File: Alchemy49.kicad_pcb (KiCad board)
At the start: 2 copper layers, 267.5 x 76.2 mm, 255 parts, among them J1 USB_B_Micro, J2 Conn_01x05_Female, Q1 2N7002E, SW1 ESC-1.5U, SW10 O-1U, SW11 P-1U, SW12 BACK-1.5U, SW13 DEL-1U, SW14 TAB-1.75U, SW15 A-1U, SW16 S-1U, SW17 D-1U, SW18 F-1U, SW19 G-1U, SW2 Q-1U, SW20 H-1U, SW21 J-1U, SW22 K-1U, SW23 L-1U, SW24 ENTER-2.25U, SW25 PGUP-1U, SW26 SHIFT-2U, SW27 Z-1U, SW28 X-1U, SW29 C-1U, SW3 W-1U, SW30 V-1U, SW31 B-1U, SW32 N-1U, SW33 M-1U, SW34 COM-1U, SW35 PER-1U, SW36 SLASH-1U, SW37 UP-1U, SW38 PGDN-1U, SW39 CTRL1-1U, SW4 E-1U, SW40 WIN-1U, SW41 ALT-1U, SW42 FN1-1U, SW43 SPACE-2.75U, SW44 SHIFT-2.25U, SW45 FN2-1U, SW46 CTRL2-1U, SW47 LEFT-1U, SW48 DOWN-1U, SW49 RIGHT-1U, SW5 R-1U, SW6 T-1U, SW7 Y-1U, SW8 U-1U, SW9 I-1U

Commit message: Prototype Adjustments
* Added working KBFirmware config and hex files.
* Added example AVRDUDESS screenshot
* Added datasheet and part numbers to sch
* Adjusted pcb outlin and holes
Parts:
- removed H1, H2: MountingHole_Pad, MountingHole:MountingHole_3.5mm_Pad_Via
- moved D39 0.90 mm to (32.0, 74.5)
- moved J1 0.20 mm to (40.2, 26.5)
- moved J2 0.20 mm to (40.2, 32.5)
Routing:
- net Row1: track 298.9 -> 301.5 mm
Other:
- outline, holes or cut-outs redrawn
- board text added: "B"
- board text added: "G"
- board text added: "R"
- board text added: "Sh"
- board text added: "W"

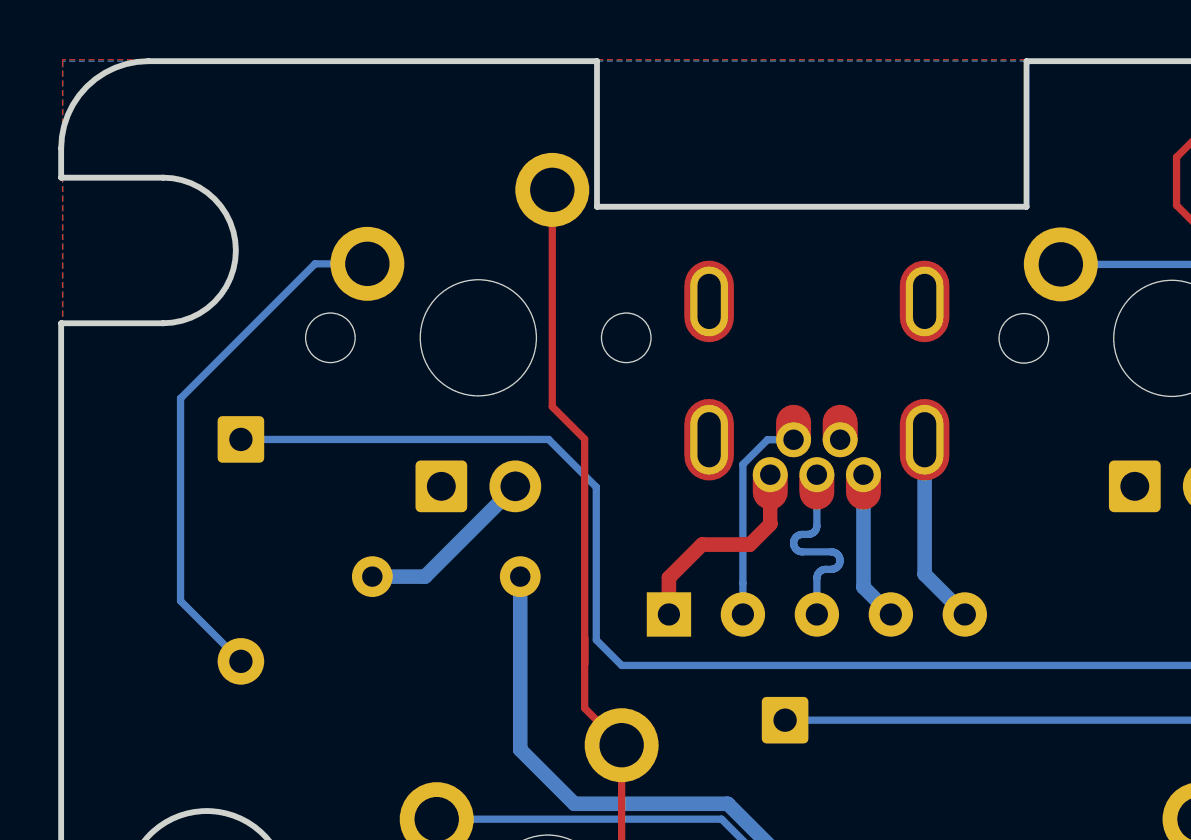
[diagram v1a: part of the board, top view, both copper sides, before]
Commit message: Cut layer adjustments for final
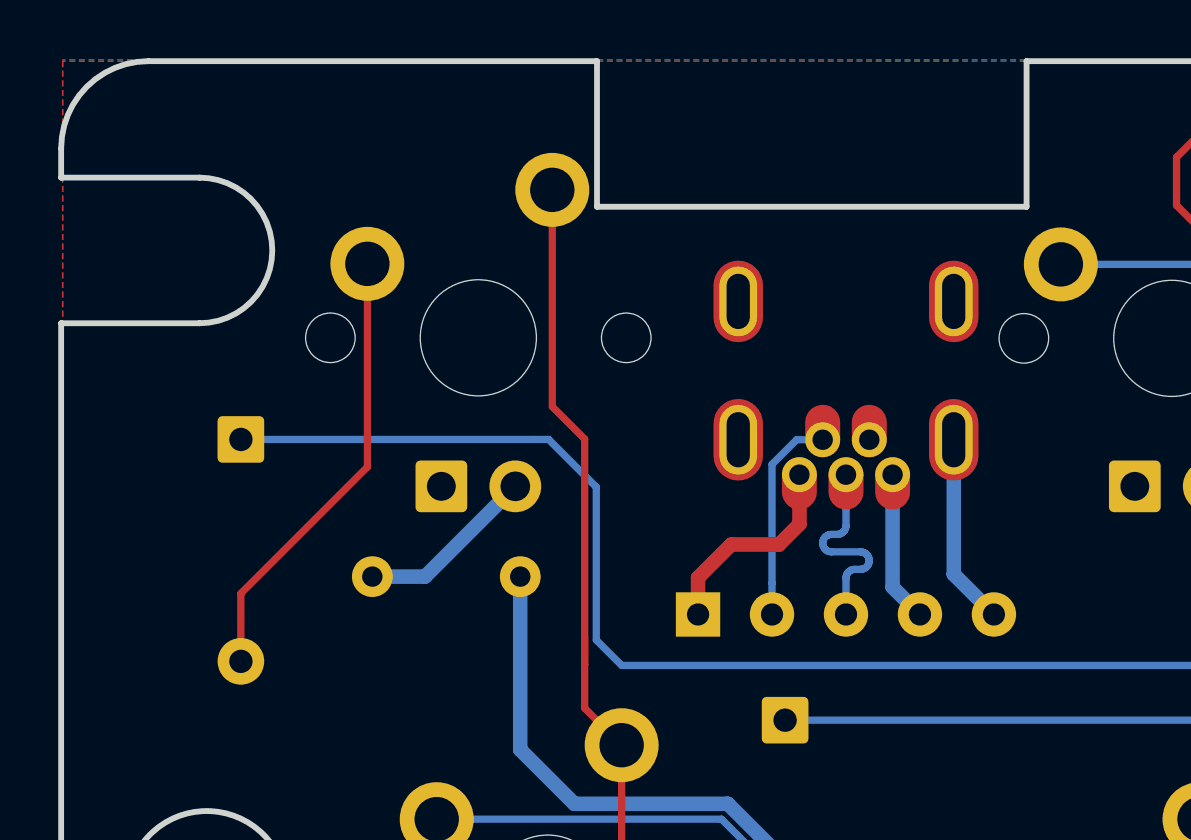
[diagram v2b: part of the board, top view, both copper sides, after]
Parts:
- moved J1 1.00 mm to (41.2, 26.5)
- moved J2 1.00 mm to (41.2, 32.5)
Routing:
- net Net-(D1-Pad2): track 18.2 -> 15.4 mm
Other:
- outline, holes or cut-outs redrawn

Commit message: OSHWA Certification
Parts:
- added OSHW_Mono_0.25_Scale: US000215, Alchemy49:OSHW_Mono_0.25_Scale, B.Cu at (102.4, 78.6)
- added REF**: OSHW-Logo_7.5x8mm_SilkScreen, Symbol:OSHW-Logo_7.5x8mm_SilkScreen, B.Cu at (177.1, 79.7)

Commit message: EvvL Logo
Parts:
- removed the REF** at (177.1, 79.7)
- added G***: LOGO, Alchemy49:EvvL, B.Cu at (146.1, 83.9)

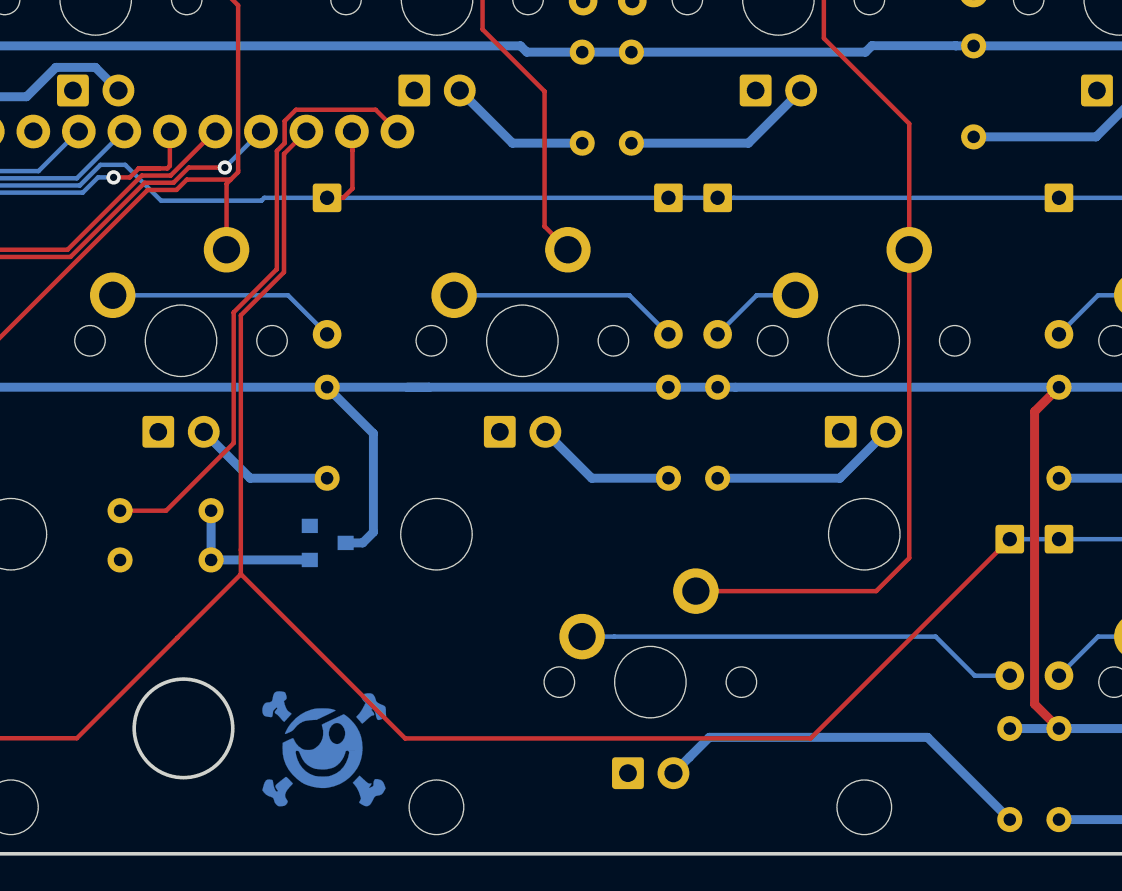
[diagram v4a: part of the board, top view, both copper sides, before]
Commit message: Changed MOSFET to FDS6630A
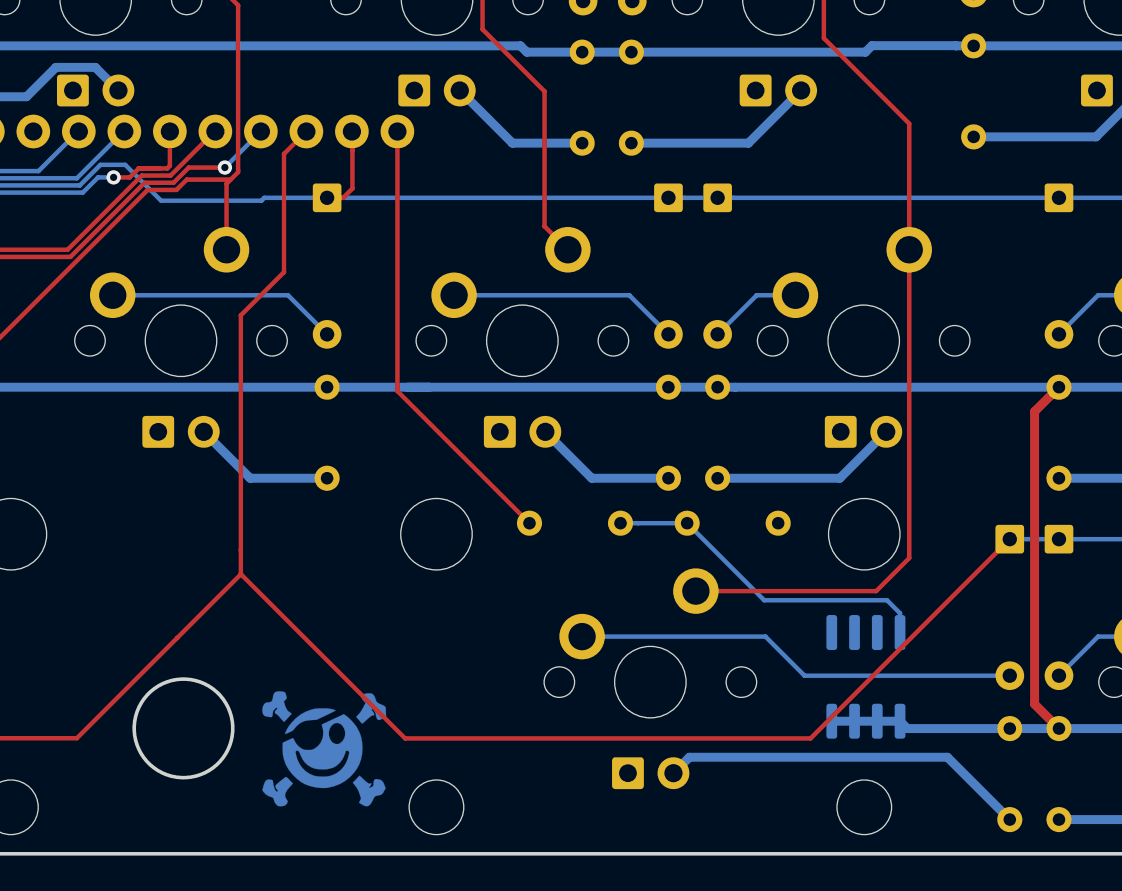
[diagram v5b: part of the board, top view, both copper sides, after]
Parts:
- B1: value >VALUE -> SPARKFUN_PRO_MICRO; footprint SparkFun_Boards:SPARKFUN_PRO_MICRO -> SPARKFUN_PRO_MICRO
- Q1: value 2N7002E -> FDS6630A; footprint Package_TO_SOT_SMD:SOT-23 -> Package_SO:SOIC-8_3.9x4.9mm_P1.27mm
- moved R51 31.7 mm to (168.9, 71.3), turned to 180 degrees
- moved Q1 31.0 mm to (176.3, 79.9), turned to 270 degrees
- moved R50 22.9 mm to (160.1, 71.3)
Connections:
- Q1 pad 1: Net-(Q1-Pad1) -> GND
- Q1 pad 3: LED -> GND
- R50 pad 1: Net-(Q1-Pad1) -> Net-(Q1-Pad4)
- R51 pad 2: Net-(Q1-Pad1) -> Net-(Q1-Pad4)
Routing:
- net Net-(Q1-Pad4): track 0.00 -> 18.8 mm
- net LEDCTL: track 34.1 -> 24.9 mm
- net Net-(Q1-Pad1): track 8.26 -> 0.00 mm
- net Net-(LED44-PadA): track 21.5 -> 20.6 mm
- net LED: track 889.8 -> 888.9 mm

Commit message: flipped the leds around the correct way
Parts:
- moved REF** 0.95 mm to (140.2, 76.7)
- moved G*** 0.74 mm to (145.9, 84.6)
- turned LED1 to 0 degrees
- turned LED10 to 0 degrees
- turned LED11 to 0 degrees
- turned LED12 to 0 degrees
- turned LED13 to 0 degrees
- turned LED14 to 0 degrees
- turned LED15 to 0 degrees
- turned LED16 to 0 degrees
- turned LED17 to 0 degrees
- turned LED18 to 0 degrees
- turned LED19 to 0 degrees
- turned LED2 to 0 degrees
- turned LED20 to 0 degrees
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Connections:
- LED1 pad A: Net-(LED1-PadA) -> VCC
- LED1 pad K: VCC -> Net-(LED1-PadK)
- LED10 pad A: Net-(LED10-PadA) -> VCC
- LED10 pad K: VCC -> Net-(LED10-PadK)
- LED11 pad A: Net-(LED11-PadA) -> VCC
- LED11 pad K: VCC -> Net-(LED11-PadK)
- LED12 pad A: Net-(LED12-PadA) -> VCC
- LED12 pad K: VCC -> Net-(LED12-PadK)
- LED13 pad A: Net-(LED13-PadA) -> VCC
- LED13 pad K: VCC -> Net-(LED13-PadK)
- LED14 pad A: Net-(LED14-PadA) -> VCC
- LED14 pad K: VCC -> Net-(LED14-PadK)
- LED15 pad A: Net-(LED15-PadA) -> VCC
- LED15 pad K: VCC -> Net-(LED15-PadK)
- LED16 pad A: Net-(LED16-PadA) -> VCC
- LED16 pad K: VCC -> Net-(LED16-PadK)
- LED17 pad A: Net-(LED17-PadA) -> VCC
- LED17 pad K: VCC -> Net-(LED17-PadK)
- LED18 pad A: Net-(LED18-PadA) -> VCC
- LED18 pad K: VCC -> Net-(LED18-PadK)
- LED19 pad A: Net-(LED19-PadA) -> VCC
- LED19 pad K: VCC -> Net-(LED19-PadK)
- LED2 pad A: Net-(LED2-PadA) -> VCC
- LED2 pad K: VCC -> Net-(LED2-PadK)
- LED20 pad A: Net-(LED20-PadA) -> VCC
- LED20 pad K: VCC -> Net-(LED20-PadK)
- LED21 pad A: Net-(LED21-PadA) -> VCC
- LED21 pad K: VCC -> Net-(LED21-PadK)
- LED22 pad A: Net-(LED22-PadA) -> VCC
- LED22 pad K: VCC -> Net-(LED22-PadK)
- LED23 pad A: Net-(LED23-PadA) -> VCC
- LED23 pad K: VCC -> Net-(LED23-PadK)
- LED24 pad A: Net-(LED24-PadA) -> VCC
- LED24 pad K: VCC -> Net-(LED24-PadK)
- LED25 pad A: Net-(LED25-PadA) -> VCC
- LED25 pad K: VCC -> Net-(LED25-PadK)
- LED26 pad A: Net-(LED26-PadA) -> VCC
- LED26 pad K: VCC -> Net-(LED26-PadK)
- LED27 pad A: Net-(LED27-PadA) -> VCC
- LED27 pad K: VCC -> Net-(LED27-PadK)
- LED28 pad A: Net-(LED28-PadA) -> VCC
- LED28 pad K: VCC -> Net-(LED28-PadK)
- LED29 pad A: Net-(LED29-PadA) -> VCC
- LED29 pad K: VCC -> Net-(LED29-PadK)
- LED3 pad A: Net-(LED3-PadA) -> VCC
- LED3 pad K: VCC -> Net-(LED3-PadK)
- LED30 pad A: Net-(LED30-PadA) -> VCC
- LED30 pad K: VCC -> Net-(LED30-PadK)
- LED31 pad A: Net-(LED31-PadA) -> VCC
- LED31 pad K: VCC -> Net-(LED31-PadK)
- LED32 pad A: Net-(LED32-PadA) -> VCC
- LED32 pad K: VCC -> Net-(LED32-PadK)
- LED33 pad A: Net-(LED33-PadA) -> VCC
- LED33 pad K: VCC -> Net-(LED33-PadK)
- LED34 pad A: Net-(LED34-PadA) -> VCC
- LED34 pad K: VCC -> Net-(LED34-PadK)
- LED35 pad A: Net-(LED35-PadA) -> VCC
- LED35 pad K: VCC -> Net-(LED35-PadK)
- LED36 pad A: Net-(LED36-PadA) -> VCC
- LED36 pad K: VCC -> Net-(LED36-PadK)
- LED37 pad A: Net-(LED37-PadA) -> VCC
- LED37 pad K: VCC -> Net-(LED37-PadK)
- LED38 pad A: Net-(LED38-PadA) -> VCC
- LED38 pad K: VCC -> Net-(LED38-PadK)
- LED39 pad A: Net-(LED39-PadA) -> VCC
- LED39 pad K: VCC -> Net-(LED39-PadK)
- LED4 pad A: Net-(LED4-PadA) -> VCC
- LED4 pad K: VCC -> Net-(LED4-PadK)
- LED40 pad A: Net-(LED40-PadA) -> VCC
- LED40 pad K: VCC -> Net-(LED40-PadK)
- LED41 pad A: Net-(LED41-PadA) -> VCC
- LED41 pad K: VCC -> Net-(LED41-PadK)
- LED42 pad A: Net-(LED42-PadA) -> VCC
- LED42 pad K: VCC -> Net-(LED42-PadK)
- LED43 pad A: Net-(LED43-PadA) -> VCC
- LED43 pad K: VCC -> Net-(LED43-PadK)
- LED44 pad A: Net-(LED44-PadA) -> VCC
- LED44 pad K: VCC -> Net-(LED44-PadK)
- LED45 pad A: Net-(LED45-PadA) -> VCC
- LED45 pad K: VCC -> Net-(LED45-PadK)
- LED46 pad A: Net-(LED46-PadA) -> VCC
- LED46 pad K: VCC -> Net-(LED46-PadK)
- LED47 pad A: Net-(LED47-PadA) -> VCC
- LED47 pad K: VCC -> Net-(LED47-PadK)
- LED48 pad A: Net-(LED48-PadA) -> VCC
- LED48 pad K: VCC -> Net-(LED48-PadK)
- LED49 pad A: Net-(LED49-PadA) -> VCC
- LED49 pad K: VCC -> Net-(LED49-PadK)
- LED5 pad A: Net-(LED5-PadA) -> VCC
- LED5 pad K: VCC -> Net-(LED5-PadK)
- LED6 pad A: Net-(LED6-PadA) -> VCC
- LED6 pad K: VCC -> Net-(LED6-PadK)
- LED7 pad A: Net-(LED7-PadA) -> VCC
- LED7 pad K: VCC -> Net-(LED7-PadK)
- LED8 pad A: Net-(LED8-PadA) -> VCC
- LED8 pad K: VCC -> Net-(LED8-PadK)
- LED9 pad A: Net-(LED9-PadA) -> VCC
- LED9 pad K: VCC -> Net-(LED9-PadK)
- R1 pad 1: Net-(LED1-PadA) -> Net-(LED1-PadK)
- R10 pad 1: Net-(LED10-PadA) -> Net-(LED10-PadK)
- R11 pad 1: Net-(LED11-PadA) -> Net-(LED11-PadK)
- R12 pad 1: Net-(LED12-PadA) -> Net-(LED12-PadK)
- R13 pad 1: Net-(LED13-PadA) -> Net-(LED13-PadK)
- R14 pad 1: Net-(LED14-PadA) -> Net-(LED14-PadK)
- R15 pad 1: Net-(LED15-PadA) -> Net-(LED15-PadK)
- R16 pad 1: Net-(LED16-PadA) -> Net-(LED16-PadK)
- R17 pad 1: Net-(LED17-PadA) -> Net-(LED17-PadK)
- R18 pad 1: Net-(LED18-PadA) -> Net-(LED18-PadK)
- R19 pad 1: Net-(LED19-PadA) -> Net-(LED19-PadK)
- R2 pad 1: Net-(LED2-PadA) -> Net-(LED2-PadK)
- R20 pad 1: Net-(LED20-PadA) -> Net-(LED20-PadK)
- R21 pad 1: Net-(LED21-PadA) -> Net-(LED21-PadK)
- R22 pad 1: Net-(LED22-PadA) -> Net-(LED22-PadK)
- R23 pad 1: Net-(LED23-PadA) -> Net-(LED23-PadK)
- R24 pad 1: Net-(LED24-PadA) -> Net-(LED24-PadK)
- R25 pad 1: Net-(LED25-PadA) -> Net-(LED25-PadK)
- R26 pad 1: Net-(LED26-PadA) -> Net-(LED26-PadK)
- R27 pad 1: Net-(LED27-PadA) -> Net-(LED27-PadK)
- R28 pad 1: Net-(LED28-PadA) -> Net-(LED28-PadK)
- R29 pad 1: Net-(LED29-PadA) -> Net-(LED29-PadK)
- R3 pad 1: Net-(LED3-PadA) -> Net-(LED3-PadK)
- R30 pad 1: Net-(LED30-PadA) -> Net-(LED30-PadK)
- R31 pad 1: Net-(LED31-PadA) -> Net-(LED31-PadK)
- R32 pad 1: Net-(LED32-PadA) -> Net-(LED32-PadK)
- R33 pad 1: Net-(LED33-PadA) -> Net-(LED33-PadK)
- R34 pad 1: Net-(LED34-PadA) -> Net-(LED34-PadK)
- R35 pad 1: Net-(LED35-PadA) -> Net-(LED35-PadK)
- R36 pad 1: Net-(LED36-PadA) -> Net-(LED36-PadK)
- R37 pad 1: Net-(LED37-PadA) -> Net-(LED37-PadK)
- R38 pad 1: Net-(LED38-PadA) -> Net-(LED38-PadK)
- R39 pad 1: Net-(LED39-PadA) -> Net-(LED39-PadK)
- R4 pad 1: Net-(LED4-PadA) -> Net-(LED4-PadK)
- R40 pad 1: Net-(LED40-PadA) -> Net-(LED40-PadK)
- R41 pad 1: Net-(LED41-PadA) -> Net-(LED41-PadK)
- R42 pad 1: Net-(LED42-PadA) -> Net-(LED42-PadK)
- R43 pad 1: Net-(LED43-PadA) -> Net-(LED43-PadK)
- R44 pad 1: Net-(LED44-PadA) -> Net-(LED44-PadK)
- R45 pad 1: Net-(LED45-PadA) -> Net-(LED45-PadK)
- R46 pad 1: Net-(LED46-PadA) -> Net-(LED46-PadK)
- R47 pad 1: Net-(LED47-PadA) -> Net-(LED47-PadK)
- R48 pad 1: Net-(LED48-PadA) -> Net-(LED48-PadK)
- R49 pad 1: Net-(LED49-PadA) -> Net-(LED49-PadK)
- R5 pad 1: Net-(LED5-PadA) -> Net-(LED5-PadK)
- R6 pad 1: Net-(LED6-PadA) -> Net-(LED6-PadK)
- R7 pad 1: Net-(LED7-PadA) -> Net-(LED7-PadK)
- R8 pad 1: Net-(LED8-PadA) -> Net-(LED8-PadK)
- R9 pad 1: Net-(LED9-PadA) -> Net-(LED9-PadK)
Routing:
- net Net-(LED49-PadK): track 0.00 -> 35.9 mm
- net Net-(LED49-PadA): track 35.9 -> 0.00 mm
- net Net-(LED19-PadK): track 0.00 -> 30.6 mm
- net Net-(LED19-PadA): track 30.6 -> 0.00 mm
- net Net-(LED43-PadK): track 0.00 -> 28.8 mm
- net Net-(LED43-PadA): track 28.8 -> 0.00 mm
- net Net-(LED44-PadK): track 0.00 -> 21.5 mm
- net Net-(LED44-PadA): track 20.6 -> 0.00 mm
- net Net-(LED24-PadK): track 0.00 -> 19.9 mm
- net Net-(LED24-PadA): track 19.9 -> 0.00 mm
- net Net-(LED26-PadK): track 0.00 -> 17.5 mm
- net Net-(LED26-PadA): track 17.5 -> 0.00 mm
- net Net-(LED18-PadK): track 0.00 -> 13.2 mm
- net Net-(LED18-PadA): track 13.2 -> 0.00 mm
- net Net-(LED21-PadK): track 0.00 -> 10.7 mm
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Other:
- board text added: "github.com/EvvL/Alchemy49"

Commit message: Changed MOSFET to AO3402, Removed 3D models from display
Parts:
- added G***: LOGO, Alchemy49:AcheronLibrary-Tall_PlatedOutline, B.Cu at (97.8, 78.6)
- Q1: value FDS6630A -> AO3402A; footprint Package_SO:SOIC-8_3.9x4.9mm_P1.27mm -> Package_TO_SOT_SMD:SOT-23
- moved OSHW_Mono_0.25_Scale 74.3 mm to (176.7, 78.1)
- moved Q1 50.0 mm to (128.6, 65.1), turned to 90 degrees
- moved R51 33.0 mm to (135.9, 72.1), turned to 0 degrees
- moved R50 15.3 mm to (144.8, 72.1), turned to 0 degrees
- turned LED39 to 0 degrees
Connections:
- net Net-(J1-Pad6) renamed SHLD
- Q1 pad 1: GND -> Net-(Q1-Pad1)
- Q1 pad 3: GND -> LED
- R50 pad 1: Net-(Q1-Pad4) -> Net-(Q1-Pad1)
- R51 pad 2: Net-(Q1-Pad4) -> Net-(Q1-Pad1)
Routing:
- net Net-(Q1-Pad4): track 18.8 -> 0.00 mm
- net Net-(Q1-Pad1): track 0.00 -> 15.2 mm
- net LED: track 888.9 -> 879.0 mm
- net Row4: track 255.7 -> 247.0 mm, vias 0 -> 1
- net Net-(D43-Pad2): track 21.9 -> 29.6 mm
- net Net-(LED39-PadK): track 0.00 -> 2.76 mm
- net Net-(LED39-PadA): track 2.76 -> 0.00 mm
- net LEDCTL: track 24.9 -> 25.7 mm
- net Row3: track 220.9 -> 220.3 mm
- added copper zone on B.Cu, net SHLD
